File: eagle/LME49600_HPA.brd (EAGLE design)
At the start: 100 x 80 mm, 41 parts, among them IC1 OPA2134P, IC2 OPA2134P, P1 POLYSWITCH, P2 POLYSWITCH

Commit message: bug fix
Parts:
- removed JP3, JP6: SERVO, pinhead:1X02
- added C19: 4.7uF, rcl:E2-4
- added C20: (no value), rcl:C050-055X075
- added R11, R12: 1.2k, rcl:0207/7
- C11: value 0.1uF -> (none); device rcl:C075-042X103 -> rcl:C050-055X075
- C15: value 1.0uF -> 0.1uF; device rcl:C050-050X075 -> rcl:C075-042X103
- C17: value 4.7uF -> 1.0uF; device rcl:E2-4 -> rcl:C050-050X075
- R10: value 1.2k -> 1M
- R8: value 1M -> 1.2k
- moved R1 213.7 mm to (8.89, 58.4)
- moved C11 204.5 mm to (10.2, 63.5), turned to 180 degrees
- moved C7 198.4 mm to (54.6, 63.5)
- moved C18 190.4 mm to (54.6, 2.54), turned to 180 degrees
- moved JP5 189.1 mm to (38.1, 31.8), turned to 90 degrees
- moved P1 184.2 mm to (80.0, 45.7)
- moved R7 184.2 mm to (24.1, 25.4)
- moved C15 183.2 mm to (52.1, 30.5), turned to 180 degrees
- moved R8 183.1 mm to (24.1, 27.9), turned to 180 degrees
- moved R9 183.1 mm to (25.4, 8.89), turned to 90 degrees
- moved P2 182.1 mm to (80.0, 30.5)
- moved C14 179.7 mm to (52.1, 7.62), turned to 180 degrees
- moved C13 177.8 mm to (17.8, 19.1), turned to 270 degrees
- moved R10 177.2 mm to (22.9, 8.89), turned to 90 degrees
- moved C6 177.0 mm to (54.6, 40.6), turned to 180 degrees
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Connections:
- removed net N$5 (its old number): C15.1, IC2.6, R8.2
- new net N$15: C20.2, JP4.1
- new net N$16: C20.1, IC2.3, R12.2
- new net N$4: IC2.2, R11.2, R7.2, R8.1
- net AGND: now also C15.2, C17.2, C18.-, C19.+, R12.1, R7.1, R9.1; no longer C11.2, C16.2, C17.-, C18.+, JP3.2, JP6.2, R8.1
- net N$1: now also C11.2; no longer IC1.3
- net N$10: now also C17.1, IC2.5, R10.2; no longer C15.2, IC2.7, JP6.1, R10.1
- net N$11: no longer JP3.1
- net N$12: now also C16.2, IC2.7, R11.1; no longer JP5.1, R7.2, R9.1, U$2.8
- net N$13: now also JP5.1, R10.1, R8.2, U$2.8; no longer IC2.3, JP4.1
- net N$2: now also C11.1, IC1.3; no longer IC2.2, R10.2, R7.1
- net N$9: now also IC2.6; no longer IC2.5
- net V+: now also C12.1, C14.1, C18.+; no longer C11.1, C13.1, C17.+
- net V-: now also C13.1, C15.1, C19.-; no longer C12.1, C14.1, C18.-
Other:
- board size 100 x 80 mm -> 93.7 x 71.1 mm

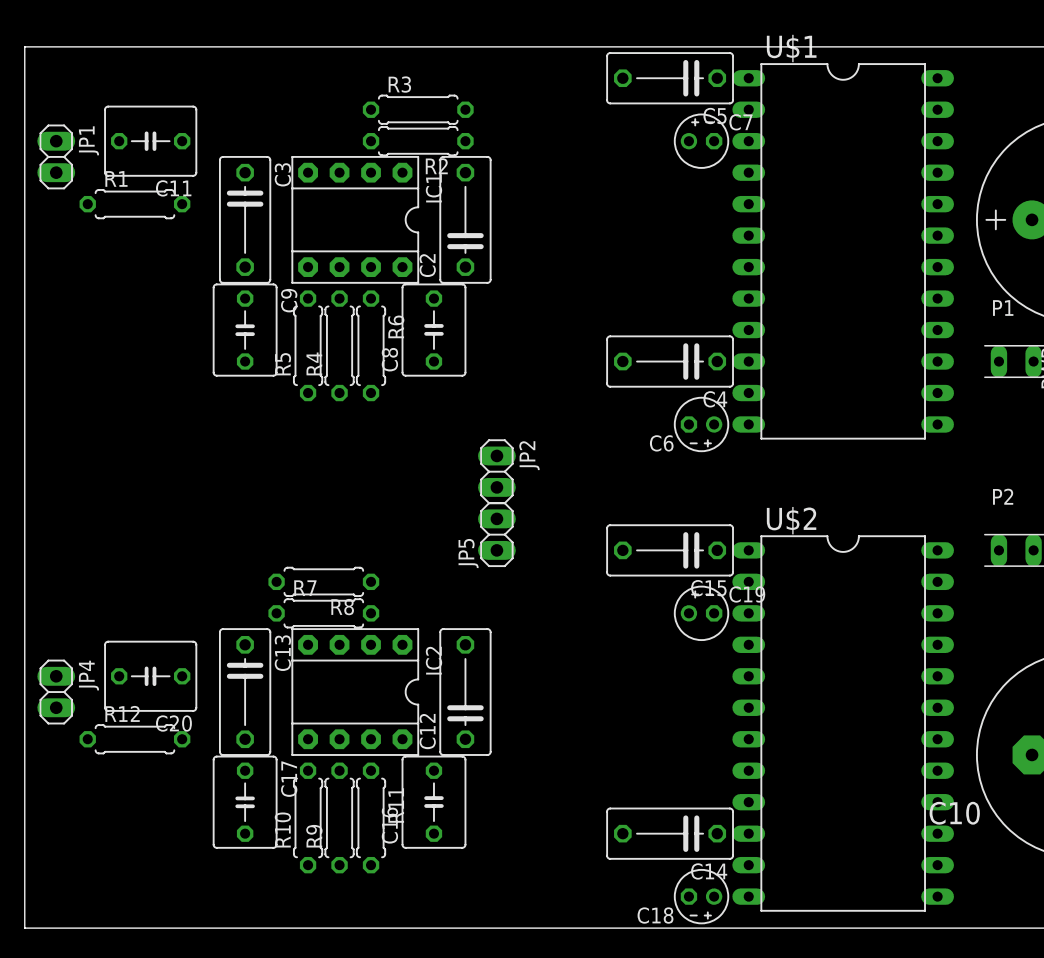
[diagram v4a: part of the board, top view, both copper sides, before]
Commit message: Change board size of LME49600
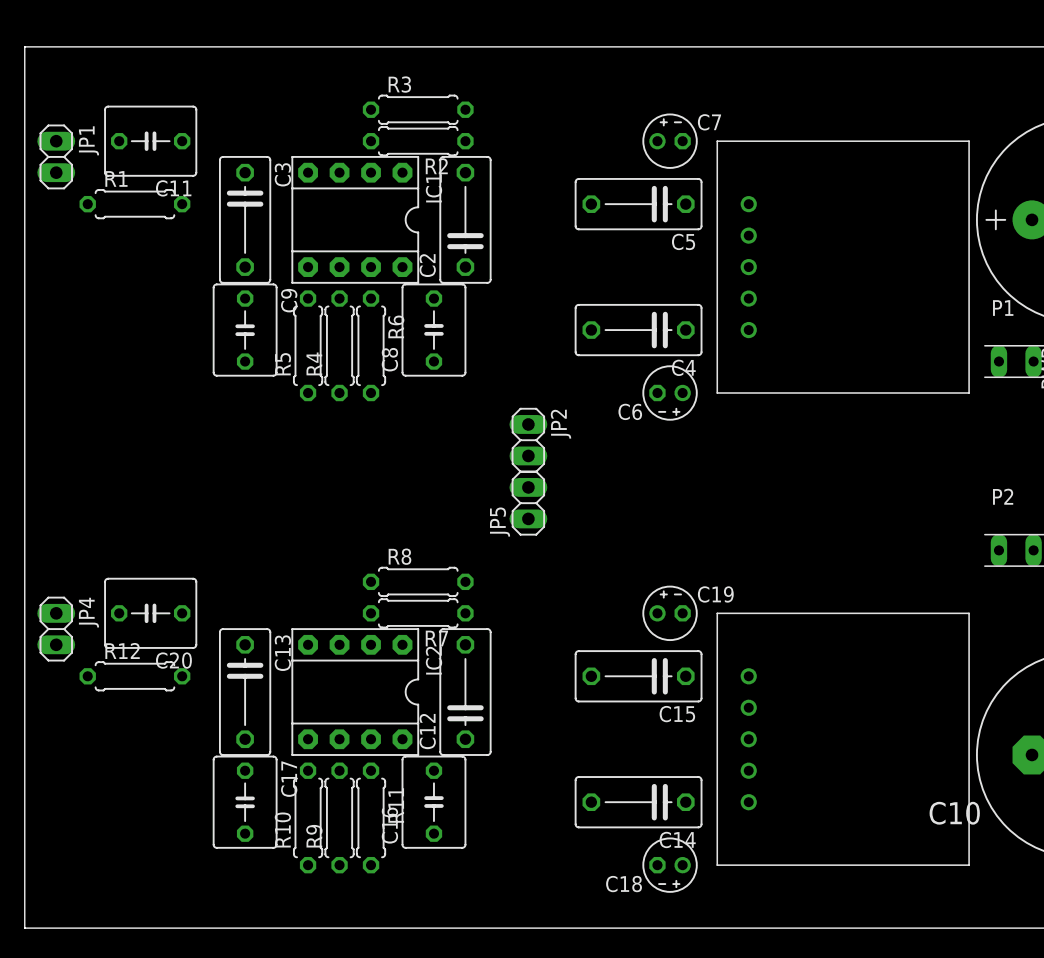
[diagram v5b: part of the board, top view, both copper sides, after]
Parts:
- U$1, U$2: value LME49600_BRD -> LME49600-BRD2; device mylib2:DIL24-6 -> mylib2:SIP5-9
- moved C15 10.5 mm to (49.5, 20.3)
- moved C5 10.5 mm to (49.5, 58.4)
- moved R7 7.62 mm to (31.8, 25.4), turned to 180 degrees
- moved R8 7.62 mm to (31.8, 27.9), turned to 0 degrees
- moved R12 5.08 mm to (8.89, 20.3)
- moved C20 5.08 mm to (10.2, 25.4)
- moved JP4 5.08 mm to (2.54, 24.1)
- moved C14 3.59 mm to (49.5, 10.2)
- moved C18 3.59 mm to (52.1, 5.08)
- moved C4 3.59 mm to (49.5, 48.3)
- moved C6 3.59 mm to (52.1, 43.2)
- moved JP2 3.59 mm to (40.6, 39.4)
- moved JP5 3.59 mm to (40.6, 34.3)
- moved U$2 2.54 mm to (66.0, 15.2)
- moved C19 2.54 mm to (52.1, 25.4)
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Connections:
- net N$13: now also U$2.P$4; no longer U$2.8
- net N$14: now also U$1.P$4; no longer U$1.8
- net N$5: now also U$2.P$2; no longer U$2.4
- net N$7: now also U$1.P$2; no longer U$1.4
- net V+: now also U$1.P$5, U$2.P$5; no longer U$1.10, U$2.10
- net V-: now also U$1.P$1, U$1.P$3, U$2.P$1, U$2.P$3; no longer U$1.2, U$1.6, U$2.2, U$2.6

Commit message: Update: Board Design
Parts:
- moved C11 5.68 mm to (12.7, 58.4)
- moved JP1 5.68 mm to (5.08, 57.1)
- moved R1 5.68 mm to (11.4, 53.3)
- moved C7 4.02 mm to (53.3, 67.3), turned to 270 degrees
- moved R4 2.54 mm to (27.9, 47.0)
- moved C1 2.54 mm to (85.1, 59.7)
- moved C2 2.54 mm to (38.1, 57.1)
- moved C3 2.54 mm to (20.3, 57.1)
- moved C5 2.54 mm to (49.5, 61.0)
- moved C8 2.54 mm to (35.6, 48.3)
- moved C9 2.54 mm to (20.3, 48.3)
- moved IC1 2.54 mm to (29.2, 57.1)
- moved JP2 2.54 mm to (43.2, 39.4)
- moved JP5 2.54 mm to (43.2, 34.3)
- moved R2 2.54 mm to (34.3, 63.5)
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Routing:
- net AGND: track 0.00 -> 167.2 mm
- net N$14: track 0.00 -> 63.1 mm
- net V-: track 0.00 -> 55.7 mm
- net N$3: track 0.00 -> 38.7 mm
- net V+: track 0.00 -> 28.6 mm
- net N$7: track 0.00 -> 26.5 mm
- net N$2: track 0.00 -> 18.8 mm
- net N$6: track 0.00 -> 12.3 mm
- net N$11: track 0.00 -> 7.62 mm
- net N$8: track 0.00 -> 7.62 mm
- net N$1: track 0.00 -> 5.08 mm

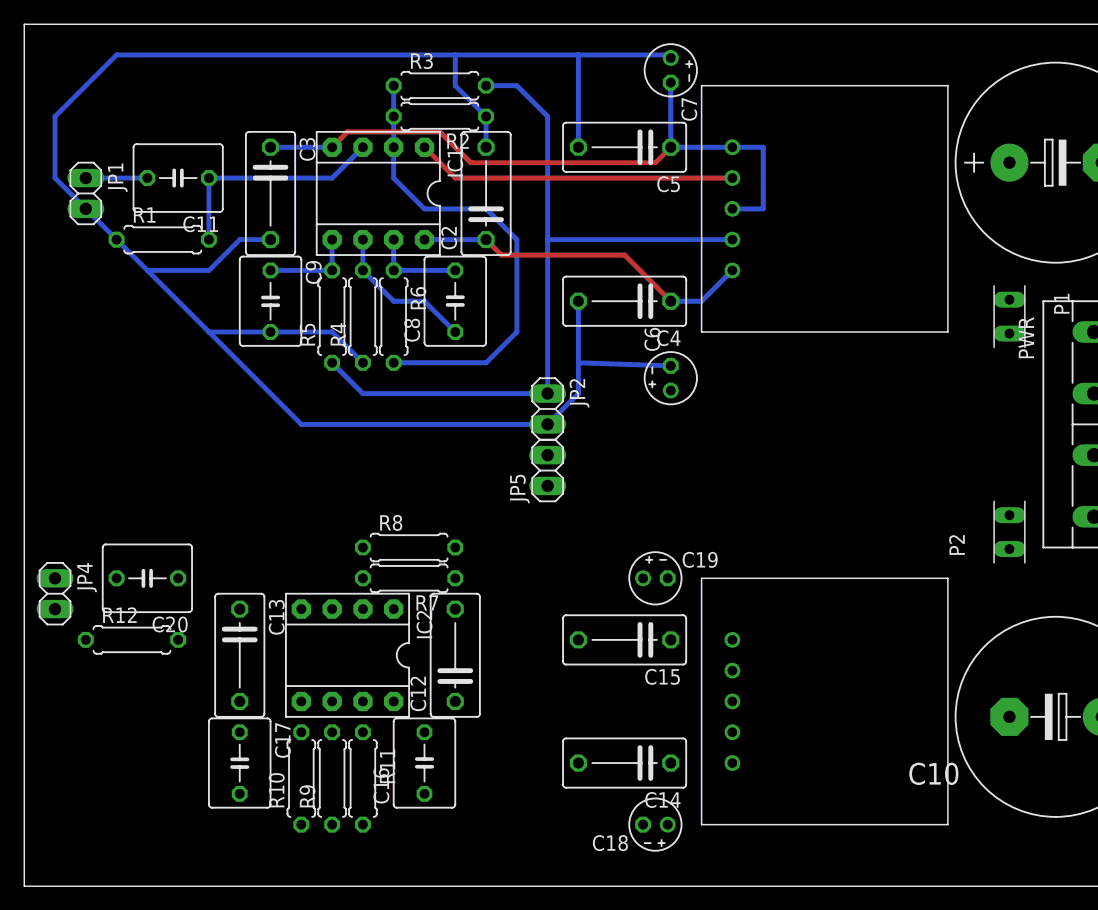
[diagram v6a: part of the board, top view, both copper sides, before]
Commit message: Change: Board size of LME49600
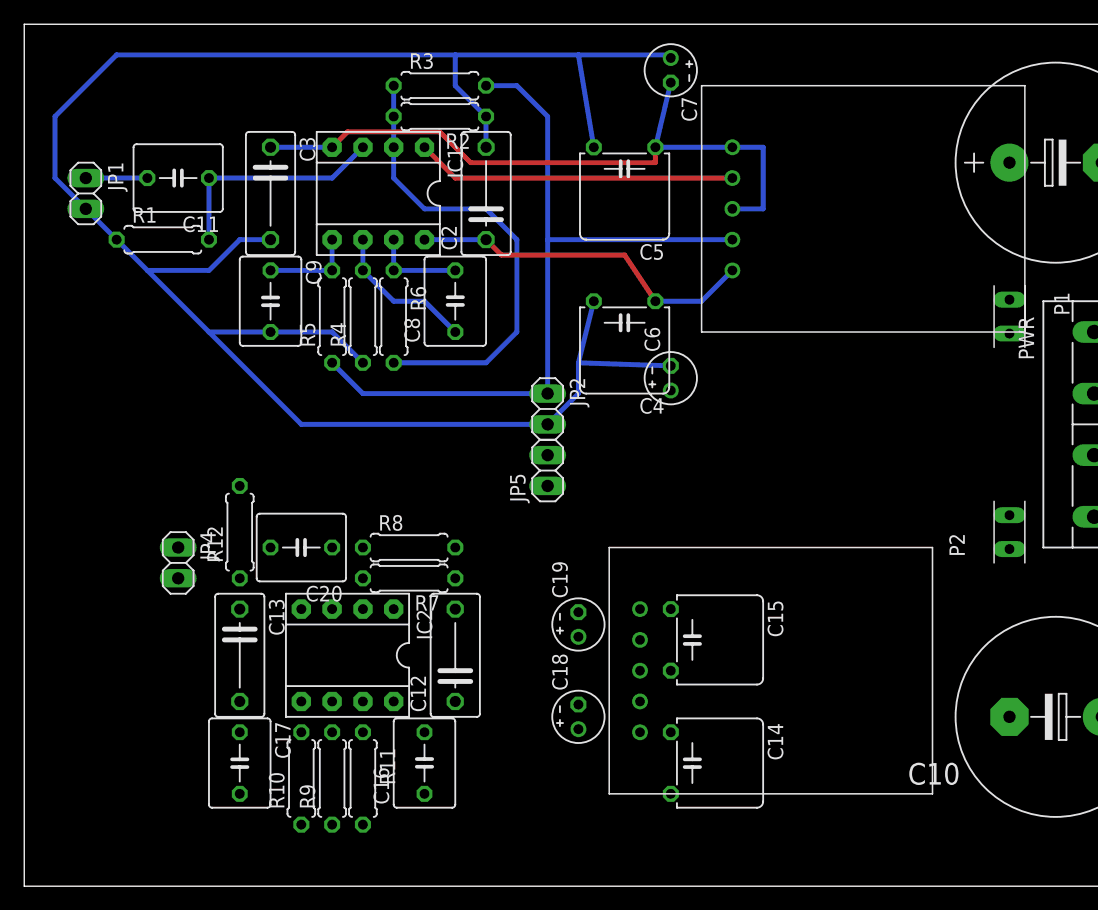
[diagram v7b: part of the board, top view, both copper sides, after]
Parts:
- C14, C15, C4, C5: device rcl:C075-042X103 -> rcl:C050H075X075
- moved C20 13.0 mm to (22.9, 27.9)
- moved R12 12.6 mm to (17.8, 29.2), turned to 90 degrees
- moved C18 10.9 mm to (45.7, 14.0), turned to 90 degrees
- moved JP4 10.5 mm to (12.7, 26.7)
- moved U$2 8.03 mm to (58.4, 17.8)
- moved C19 7.41 mm to (45.7, 21.6), turned to 90 degrees
- moved C14 3.81 mm to (53.3, 10.2), turned to 270 degrees
- moved C15 3.81 mm to (53.3, 20.3), turned to 270 degrees
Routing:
- net V-: track 55.7 -> 56.6 mm
